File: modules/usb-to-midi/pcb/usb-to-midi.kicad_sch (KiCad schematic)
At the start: 22 parts, among them J1 USB Type B Vertical, J2 Thonkiconn ST, J3 JST XH 1x2, U1 ATmega8U2-AU, Y1 16mhz

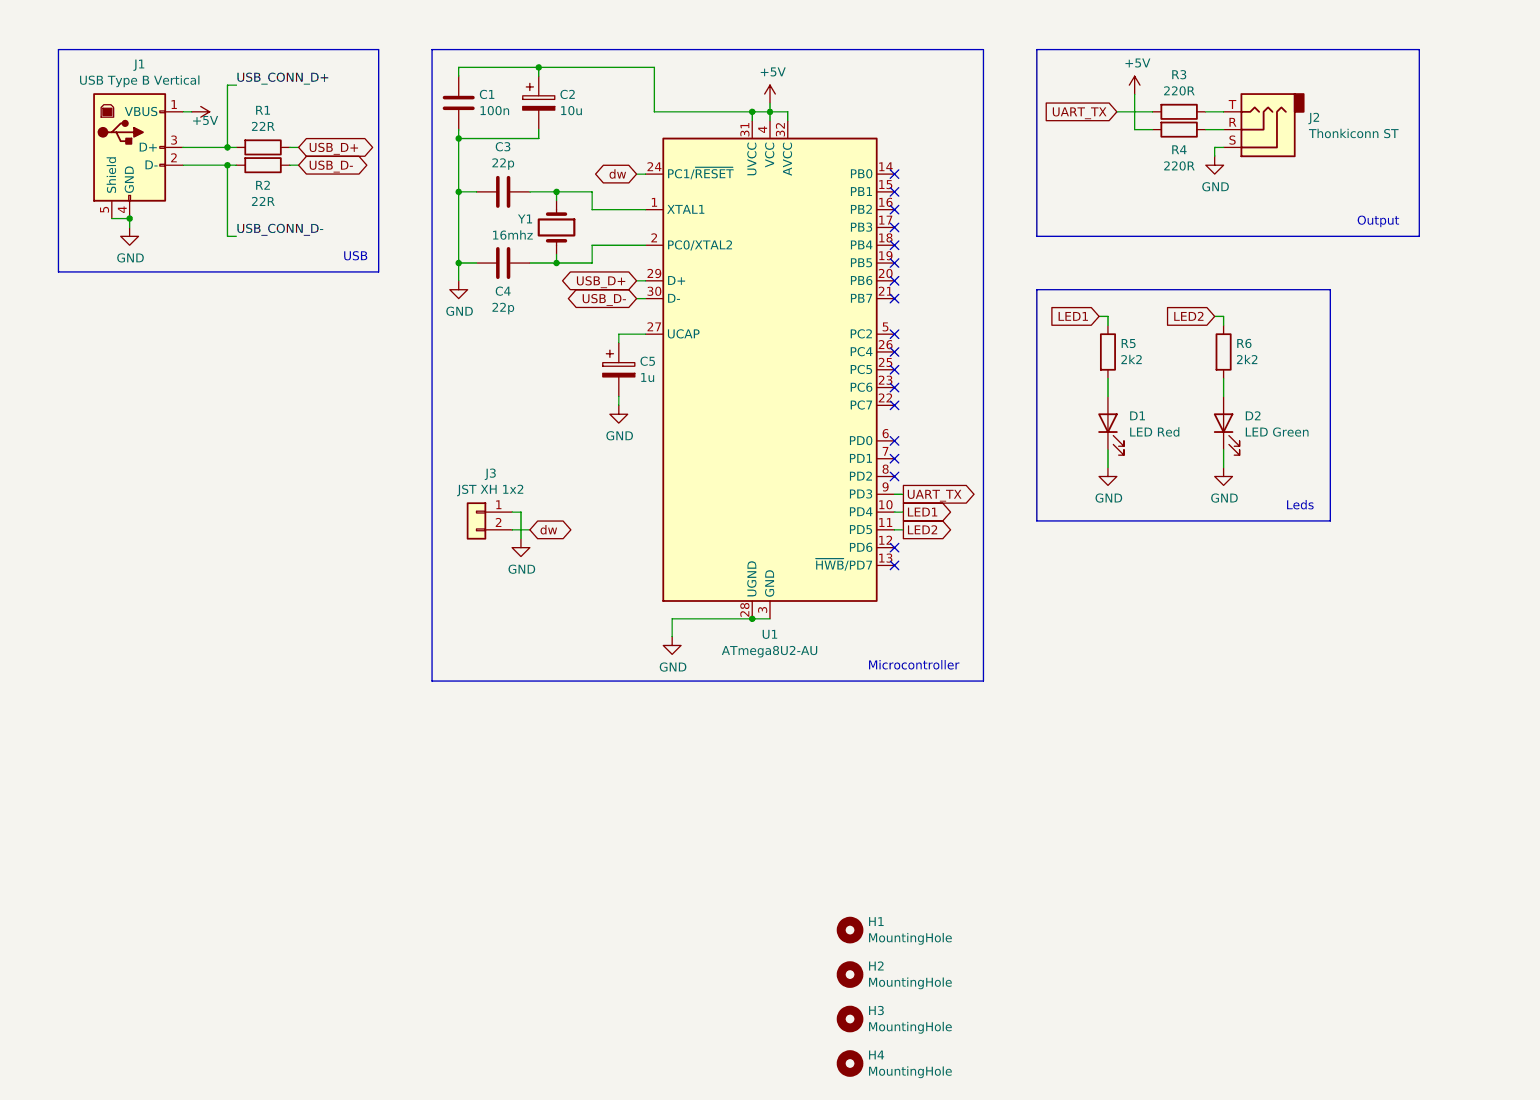
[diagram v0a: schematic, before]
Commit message: modules: usb-to-midi: revision A (redesign)
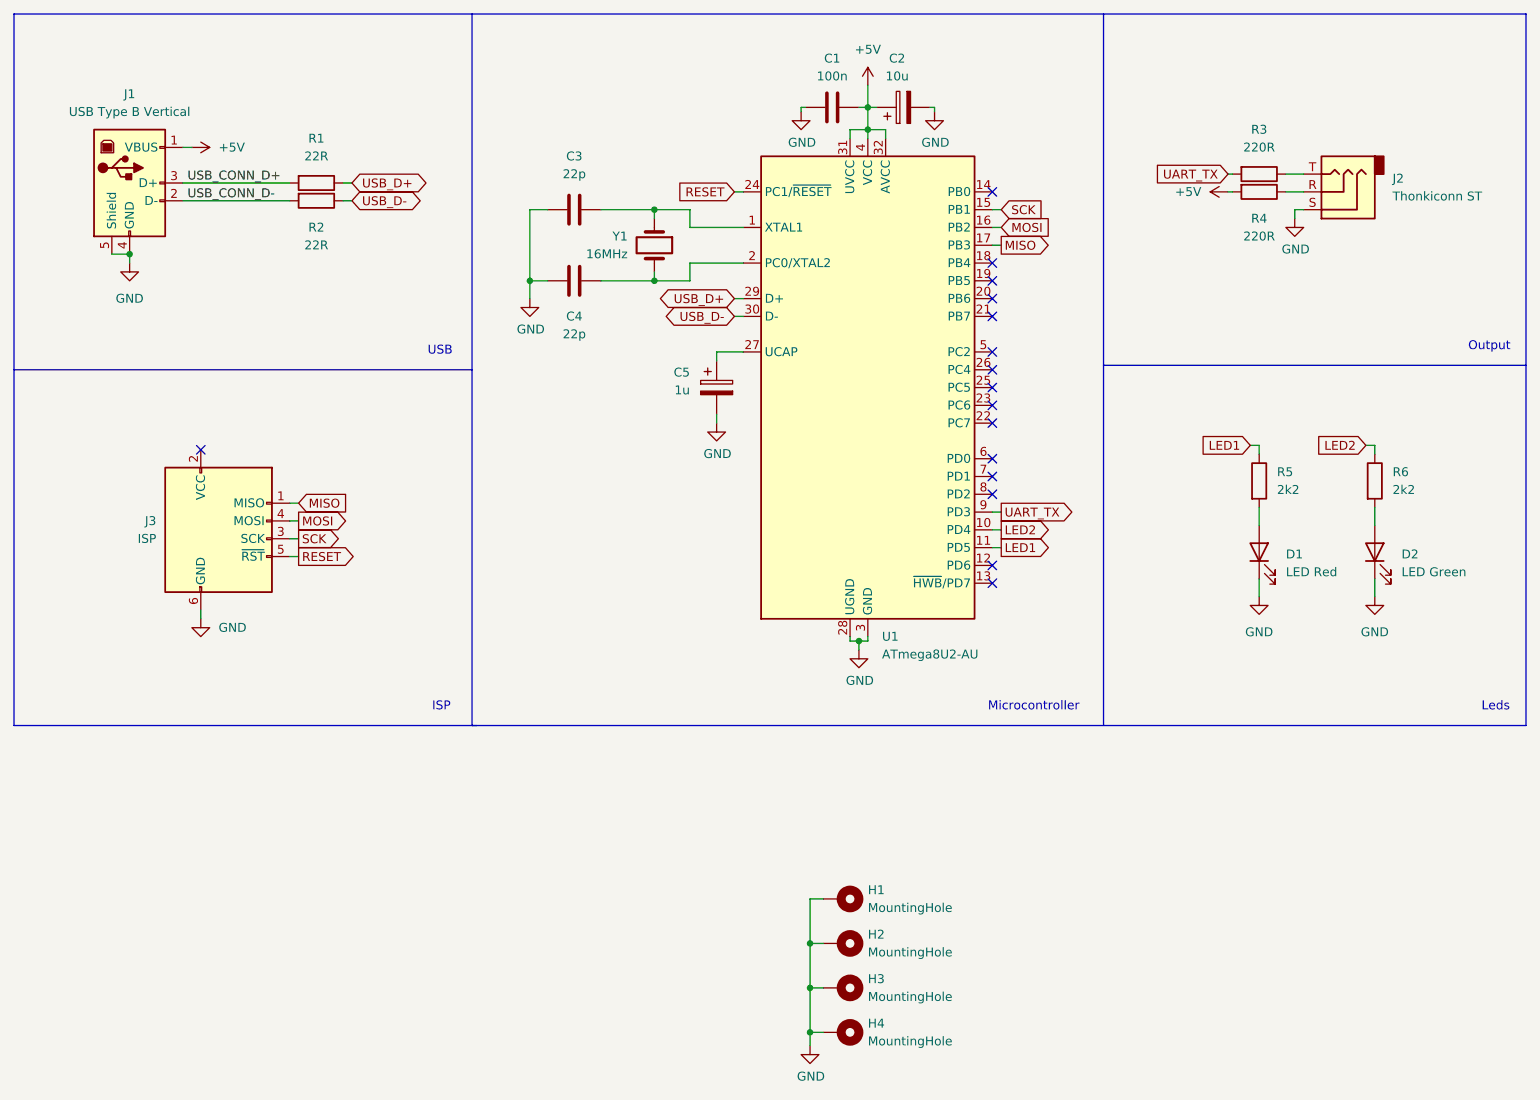
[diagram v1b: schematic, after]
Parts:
- removed J3: JST XH 1x2, Connector_JST:JST_XH_B2B-XH-A_1x02_P2.50mm_Vertical, symbol Connector_Generic:Conn_01x02
- added J3: ISP, Connector_IDC:IDC-Header_2x03_P2.54mm_Vertical, symbol Connector:AVR-ISP-6
- H1, H2, H3, H4: symbol Mechanical:MountingHole -> Mechanical:MountingHole_Pad
- J1: footprint eurorack:USB_B_Vertical -> Connector_USB:USB_B_TE_5787834_Vertical
- Y1: value 16mhz -> 16MHz
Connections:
- net +5V: now also C1.2; no longer C1.1
- net GND: now also C1.1, H1.1, H2.1, H3.1, H4.1, J3.6 (GND); no longer C1.2
- net LED1: now also U1.11 (PD5); no longer U1.10 (PD4)
- net LED2: now also U1.10 (PD4); no longer U1.11 (PD5)
- net SCK: now reaches U1.15 (PB1)
- net SCK: now also J3.3 (SCK)
- net MOSI: now reaches U1.16 (PB2)
- net MOSI: now also J3.4 (MOSI)
- net MISO: now reaches U1.17 (PB3)
- net MISO: now also J3.1 (MISO)
- net dw renamed RESET
- net RESET: now also J3.5 (~{RST})
- no-connect marks 18 -> 16
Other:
- note added: "ISP"
- company: (none) -> eurorack.rgm.io
- moved on the sheet: C1, C2, C3, C4, C5, D1, D2, J1, J2, R1, R2, R3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
